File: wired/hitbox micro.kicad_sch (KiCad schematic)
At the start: 10 parts

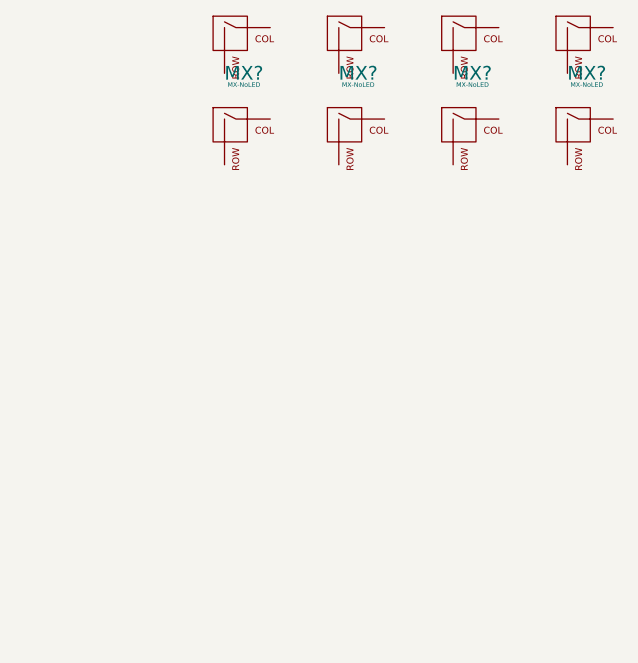
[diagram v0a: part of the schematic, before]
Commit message: Added all switches
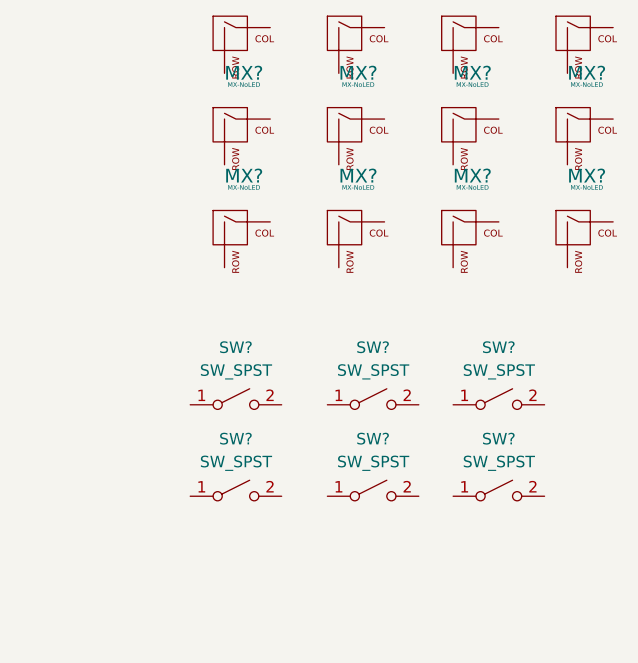
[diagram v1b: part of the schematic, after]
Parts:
- added MX? (x4): MX-NoLED, symbol MX_Alps_Hybrid:MX-NoLED
- added SW? (x6): SW_SPST, symbol Switch:SW_SPST
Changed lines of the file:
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@@
 (kicad_sch (version 20211123) (generator eeschema)
   (paper "A4")
+  (symbol (lib_id "Switch:SW_SPST") (at 142.24 104.14 0) (unit 1)
+    (in_bom yes) (on_board yes) (fields_autoplaced)
+    (property "Reference" "SW?" (id 0) (at 142.24 97.79 0))
+    (property "Value" "SW_SPST" (id 1) (at 142.24 100.33 0))
+    (property "Footprint" "" (id 2) (at 142.24 104.14 0)
+      (effects (font (size 1.27 1.27)) hide)
+    )
+    (property "Datasheet" "~" (id 3) (at 142.24 104.14 0)
+      (effects (font (size 1.27 1.27)) hide)
+    )
+    (pin "1")
+    (pin "2")
+  )
+  (symbol (lib_id "Switch:SW_SPST") (at 156.21 104.14 0) (unit 1)
+    (in_bom yes) (on_board yes) (fields_autoplaced)
+    (property "Reference" "SW?" (id 0) (at 156.21 97.79 0))
+    (property "Value" "SW_SPST" (id 1) (at 156.21 100.33 0))
+    (property "Footprint" "" (id 2) (at 156.21 104.14 0)
+      (effects (font (size 1.27 1.27)) hide)
+    )
+    (property "Datasheet" "~" (id 3) (at 156.21 104.14 0)
+      (effects (font (size 1.27 1.27)) hide)
+    )
+    (pin "1")
+    (pin "2")
+  )
   (symbol (lib_id "MX_Alps_Hybrid:MX-NoLED") (at 127 63.5 0) (unit 1)
     (in_bom yes) (on_board yes) (fields_autoplaced)
@@
     (pin "2")
   )
+  (symbol (lib_id "Switch:SW_SPST") (at 142.24 93.98 0) (unit 1)
+    (in_bom yes) (on_board yes) (fields_autoplaced)
+    (property "Reference" "SW?" (id 0) (at 142.24 87.63 0))
+    (property "Value" "SW_SPST" (id 1) (at 142.24 90.17 0))
+    (property "Footprint" "" (id 2) (at 142.24 93.98 0)
+      (effects (font (size 1.27 1.27)) hide)
+    )
+    (property "Datasheet" "~" (id 3) (at 142.24 93.98 0)
+      (effects (font (size 1.27 1.27)) hide)
+    )
+    (pin "1")
+    (pin "2")
+  )
+  (symbol (lib_id "Switch:SW_SPST") (at 127 104.14 0) (unit 1)
+    (in_bom yes) (on_board yes) (fields_autoplaced)
+    (property "Reference" "SW?" (id 0) (at 127 97.79 0))
+    (property "Value" "SW_SPST" (id 1) (at 127 100.33 0))
+    (property "Footprint" "" (id 2) (at 127 104.14 0)
+      (effects (font (size 1.27 1.27)) hide)
+    )
+    (property "Datasheet" "~" (id 3) (at 127 104.14 0)
+      (effects (font (size 1.27 1.27)) hide)
+    )
+    (pin "1")
+    (pin "2")
+  )
+  (symbol (lib_id "Switch:SW_SPST") (at 127 93.98 0) (unit 1)
+    (in_bom yes) (on_board yes) (fields_autoplaced)
+    (property "Reference" "SW?" (id 0) (at 127 87.63 0))
+    (property "Value" "SW_SPST" (id 1) (at 127 90.17 0))
+    (property "Footprint" "" (id 2) (at 127 93.98 0)
+      (effects (font (size 1.27 1.27)) hide)
+    )
+    (property "Datasheet" "~" (id 3) (at 127 93.98 0)
+      (effects (font (size 1.27 1.27)) hide)
+    )
+    (pin "1")
+    (pin "2")
+  )
   (symbol (lib_id "MX_Alps_Hybrid:MX-NoLED") (at 139.7 63.5 0) (unit 1)
     (in_bom yes) (on_board yes) (fields_autoplaced)
@@
     (property "Datasheet" "" (id 3) (at 123.825 64.135 0)
       (effects (font (size 1.524 1.524)) hide)
+    )
+    (pin "1")
+    (pin "2")
+  )
+  (symbol (lib_id "Switch:SW_SPST") (at 156.21 93.98 0) (unit 1)
+    (in_bom yes) (on_board yes) (fields_autoplaced)
+    (property "Reference" "SW?" (id 0) (at 156.21 87.63 0))
+    (property "Value" "SW_SPST" (id 1) (at 156.21 90.17 0))
+    (property "Footprint" "" (id 2) (at 156.21 93.98 0)
+      (effects (font (size 1.27 1.27)) hide)
+    )
+    (property "Datasheet" "~" (id 3) (at 156.21 93.98 0)
+      (effects (font (size 1.27 1.27)) hide)
     )
     (pin "1")
@@
     (pin "9")
   )
+  (symbol (lib_id "MX_Alps_Hybrid:MX-NoLED") (at 165.1 74.93 0) (unit 1)
+    (in_bom yes) (on_board yes) (fields_autoplaced)
+    (property "Reference" "MX?" (id 0) (at 165.9856 68.58 0)
+      (effects (font (size 1.524 1.524)))
+    )
+    (property "Value" "MX-NoLED" (id 1) (at 165.9856 69.85 0)
+      (effects (font (size 0.508 0.508)))
+    )
+    (property "Footprint" "" (id 2) (at 149.225 75.565 0)
+      (effects (font (size 1.524 1.524)) hide)
+    )
+    (property "Datasheet" "" (id 3) (at 149.225 75.565 0)
+      (effects (font (size 1.524 1.524)) hide)
+    )
+    (pin "1")
+    (pin "2")
+  )
   (symbol (lib_id "Connector:USB_C_Receptacle_USB2.0") (at 44.45 158.75 0) (unit 1)
     (in_bom yes) (on_board yes) (fields_autoplaced)
@@
     (pin "S1")
   )
+  (symbol (lib_id "MX_Alps_Hybrid:MX-NoLED") (at 127 74.93 0) (unit 1)
+    (in_bom yes) (on_board yes) (fields_autoplaced)
+    (property "Reference" "MX?" (id 0) (at 127.8856 68.58 0)
+      (effects (font (size 1.524 1.524)))
+    )
+    (property "Value" "MX-NoLED" (id 1) (at 127.8856 69.85 0)
+      (effects (font (size 0.508 0.508)))
+    )
+    (property "Footprint" "" (id 2) (at 111.125 75.565 0)
+      (effects (font (size 1.524 1.524)) hide)
+    )
+    (property "Datasheet" "" (id 3) (at 111.125 75.565 0)
+      (effects (font (size 1.524 1.524)) hide)
+    )
+    (pin "1")
+    (pin "2")
+  )
+  (symbol (lib_id "MX_Alps_Hybrid:MX-NoLED") (at 152.4 74.93 0) (unit 1)
+    (in_bom yes) (on_board yes) (fields_autoplaced)
+    (property "Reference" "MX?" (id 0) (at 153.2856 68.58 0)
+      (effects (font (size 1.524 1.524)))
+    )
+    (property "Value" "MX-NoLED" (id 1) (at 153.2856 69.85 0)
+      (effects (font (size 0.508 0.508)))
+    )
+    (property "Footprint" "" (id 2) (at 136.525 75.565 0)
+      (effects (font (size 1.524 1.524)) hide)
+    )
+    (property "Datasheet" "" (id 3) (at 136.525 75.565 0)
+      (effects (font (size 1.524 1.524)) hide)
+    )
+    (pin "1")
+    (pin "2")
+  )
   (symbol (lib_id "MX_Alps_Hybrid:MX-NoLED") (at 139.7 53.34 0) (unit 1)
     (in_bom yes) (on_board yes) (fields_autoplaced)
@@
     )
     (property "Datasheet" "" (id 3) (at 111.125 53.975 0)
+      (effects (font (size 1.524 1.524)) hide)
+    )
+    (pin "1")
+    (pin "2")
+  )
+  (symbol (lib_id "MX_Alps_Hybrid:MX-NoLED") (at 139.7 74.93 0) (unit 1)
+    (in_bom yes) (on_board yes) (fields_autoplaced)
+    (property "Reference" "MX?" (id 0) (at 140.5856 68.58 0)
+      (effects (font (size 1.524 1.524)))
+    )
+    (property "Value" "MX-NoLED" (id 1) (at 140.5856 69.85 0)
+      (effects (font (size 0.508 0.508)))
+    )
+    (property "Footprint" "" (id 2) (at 123.825 75.565 0)
+      (effects (font (size 1.524 1.524)) hide)
+    )
+    (property "Datasheet" "" (id 3) (at 123.825 75.565 0)
       (effects (font (size 1.524 1.524)) hide)
     )
@@
       (reference "MX?") (unit 1) (value "MX-NoLED") (footprint "")
     )
+    (path "/66b7cc7c-9844-453a-b185-d1e81274405c"
+      (reference "MX?") (unit 1) (value "MX-NoLED") (footprint "")
+    )
+    (path "/8284b5d1-dc54-487a-ba31-f94c3488b122"
+      (reference "MX?") (unit 1) (value "MX-NoLED") (footprint "")
+    )
+    (path "/864fef86-5ff1-4253-abce-76871e1909a0"
+      (reference "MX?") (unit 1) (value "MX-NoLED") (footprint "")
+    )
     (path "/8b255fb8-a324-4d17-895e-eb6d2116e161"
       (reference "MX?") (unit 1) (value "MX-NoLED") (footprint "")
@@
       (reference "MX?") (unit 1) (value "MX-NoLED") (footprint "")
     )
+    (path "/da4fa6a7-b46d-4fc9-88a1-e905b69290f5"
+      (reference "MX?") (unit 1) (value "MX-NoLED") (footprint "")
+    )
+    (path "/03bfbfd3-c4e9-4643-8c54-58e3e7edcf53"
+      (reference "SW?") (unit 1) (value "SW_SPST") (footprint "")
+    )
+    (path "/0ed90ea8-c8ab-4357-9142-ff078048d28a"
+      (reference "SW?") (unit 1) (value "SW_SPST") (footprint "")
+    )
+    (path "/378e7897-f5c0-43e7-b8f0-66bd81f37b88"
+      (reference "SW?") (unit 1) (value "SW_SPST") (footprint "")
+    )
+    (path "/3bac8365-bd75-4e1b-8702-cbd2a541029e"
+      (reference "SW?") (unit 1) (value "SW_SPST") (footprint "")
+    )
+    (path "/4abb007f-8721-40dd-b60e-62cc1d496d14"
+      (reference "SW?") (unit 1) (value "SW_SPST") (footprint "")
+    )
+    (path "/5095a673-36f2-4372-9675-4e8098f7e6d4"
+      (reference "SW?") (unit 1) (value "SW_SPST") (footprint "")
+    )
     (path "/63967e9f-1ddd-4b48-ad04-e44ef1c6c3ce"
